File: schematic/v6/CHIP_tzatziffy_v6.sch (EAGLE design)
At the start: 53 parts, among them J1 2X20-CHIP0.8_DRILL, J3 S2B-PH-SM4-TB, Q1 NPN-DTC114YUA, Q2 PNP-DTA114YUA, U1 LMR62421, U3 DS2431P, X1 FH12-40S-0.5SH

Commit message: changed poti pins to smaller restring, added jumper for 3.3/5/vbat for DC/DC and 3.3/5 for audio amp
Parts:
- removed C8: n.a., rcl:C-EUC0805
- removed J3: S2B-PH-SM4-TB, Keyboard v0_5:S2B-PH-SM4-TB
- removed LG, RG: LSP10, solpad:LSP10
- added BGND, CHRIN, G, VBAT: (no value), wirepad:1,6/0,8
- added CHRIN_P: CHRIN, wirepad:SMD5
- added SJ2, SJ3: (no value), SparkFun-Retired:SOLDERJUMPER_2WAYT
- L+, L-, LI, LO, R+, R-, RI, RO: value LSP10 -> (none); device solpad:LSP10 -> wirepad:1,6/0,8
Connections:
- removed net N$9: C8.1, J1.VCC-5V@1
- new net N$24: CHRIN.P, CHRIN_P.P, J1.ACIN-5V
- new net VCC-5V: J1.VCC-5V@1
- net GND: now also BGND.P, G.P; no longer C8.2, J3.2, LG.MP, RG.MP
- net N$26: now also SJ2.2
- net N$32: now also L+.P; no longer L+.MP
- net N$33: now also L-.P; no longer L-.MP
- net N$34: now also R+.P; no longer R+.MP
- net N$35: now also R-.P; no longer R-.MP
- net N$41: now also LI.P, LO.P; no longer LI.MP, LO.MP
- net N$43: now also RI.P, RO.P; no longer RI.MP, RO.MP
- net VBAT_EXT: now also VBAT.P; no longer J3.1
- net VCC3V3: now also C11.2, C12.2, C15.1, PAM1.MUTE, PAM1.PVDD, PAM1.PVDD1, PAM1.VDD, SJ3.2, SJ3.3
- net VCC5V: now also SJ2.3, SJ3.1; no longer C11.2, C12.2, C15.1, PAM1.MUTE, PAM1.PVDD, PAM1.PVDD1, PAM1.VDD
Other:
- note added: "cut here ->"

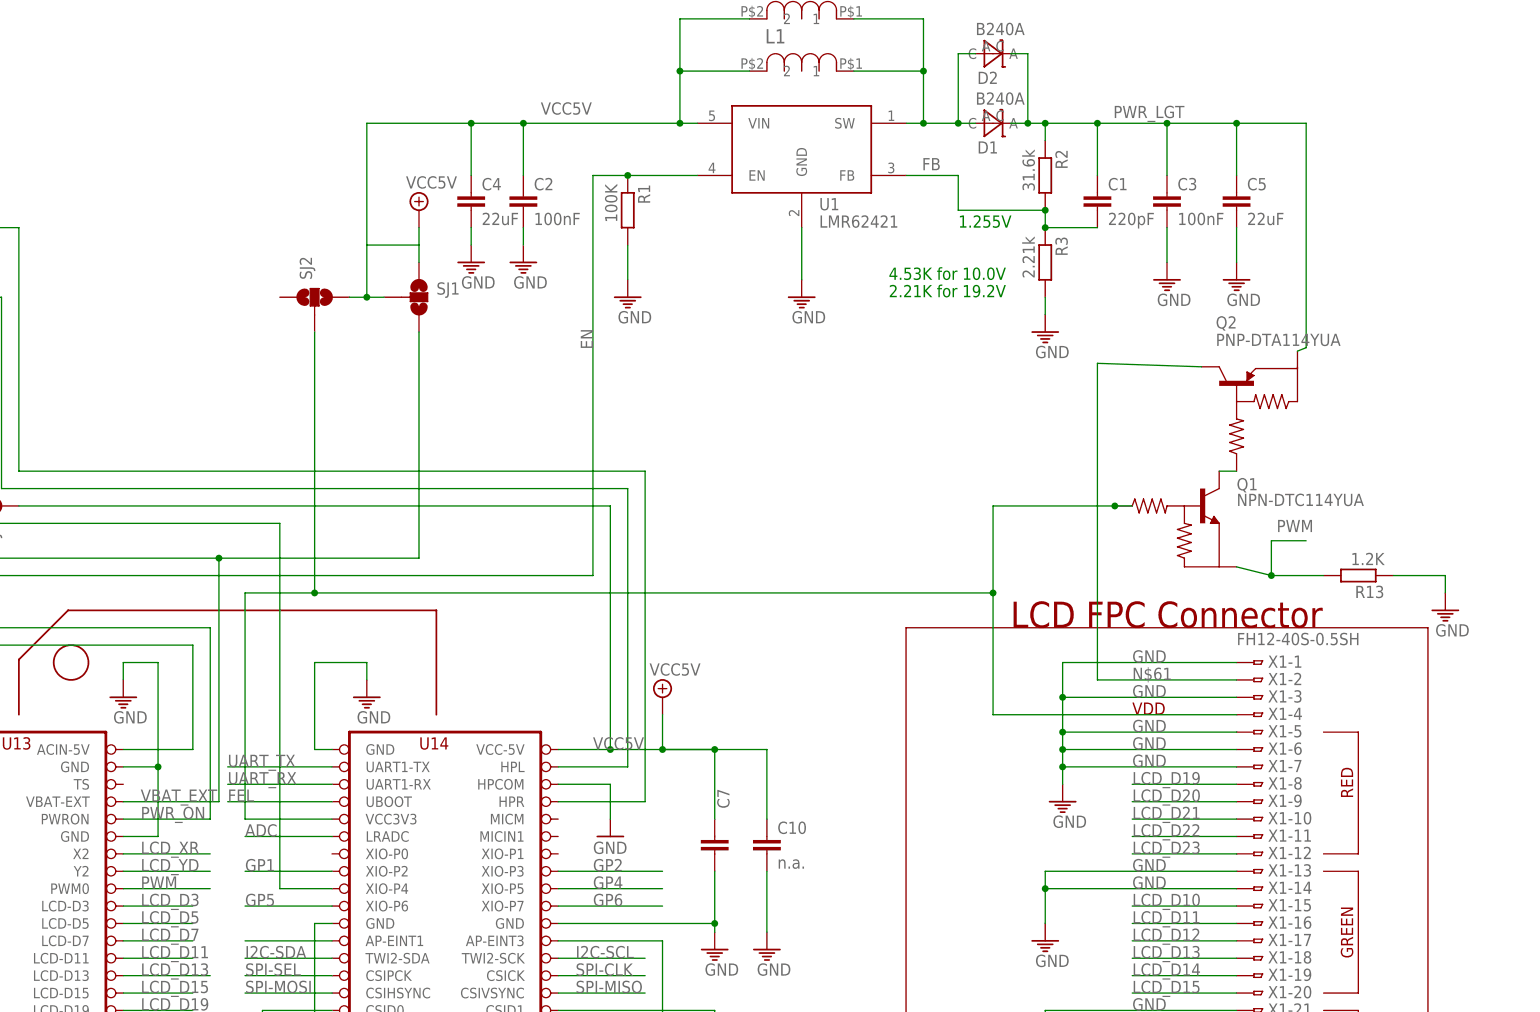
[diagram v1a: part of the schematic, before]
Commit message: replaced bipolar with mosfet circuit and relayouted
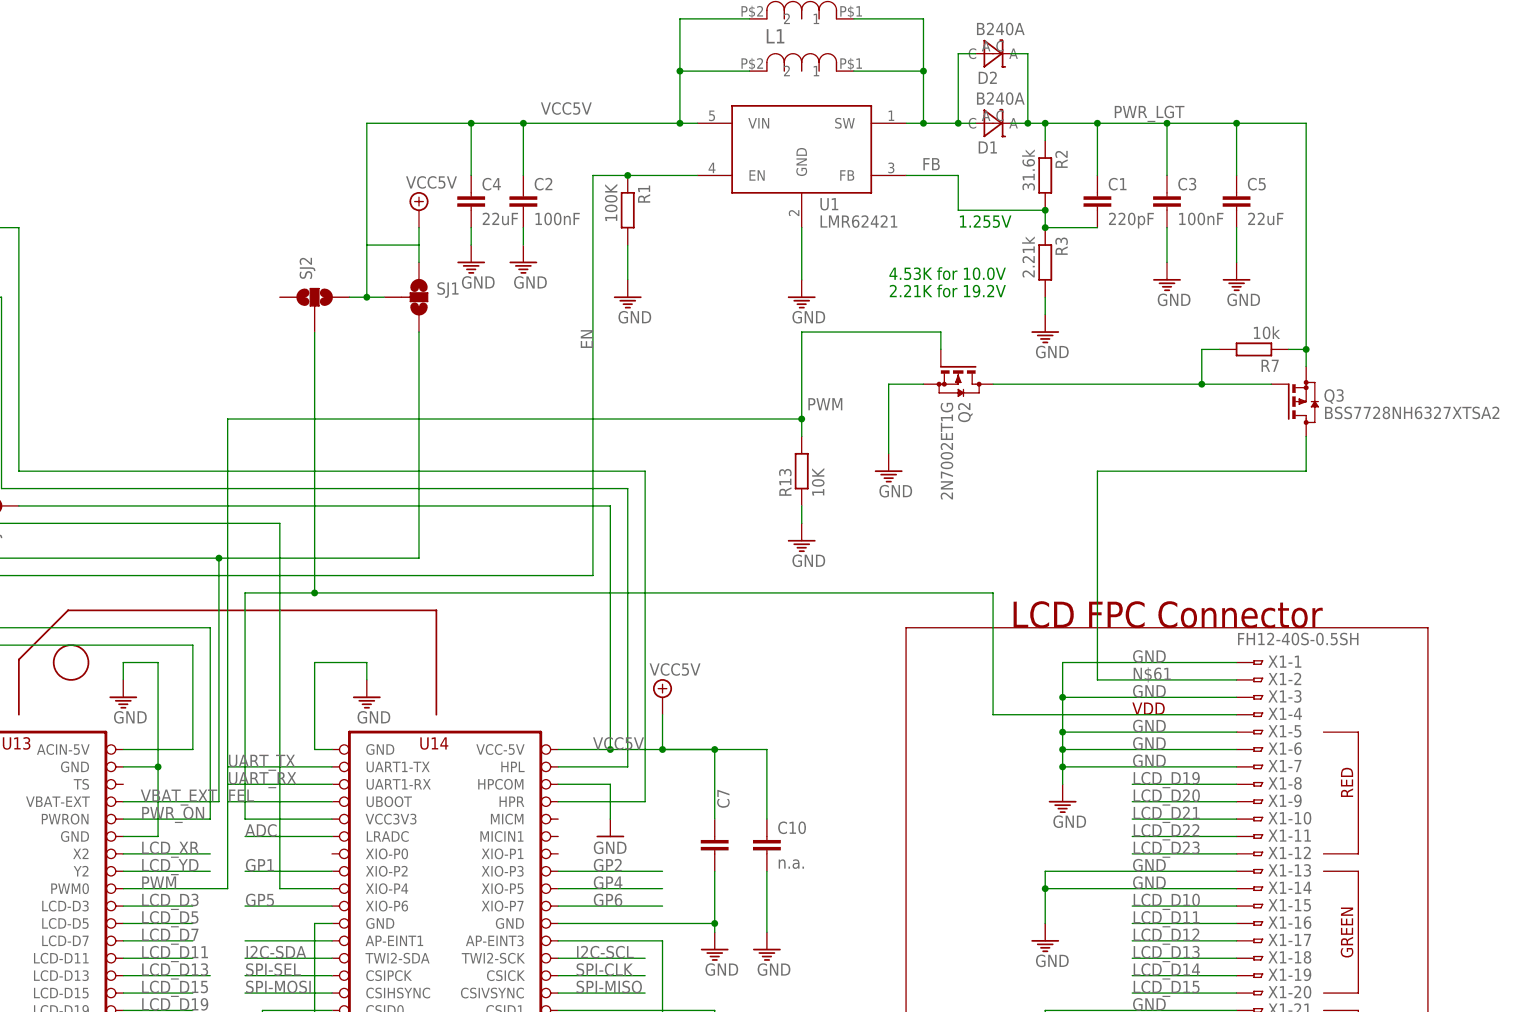
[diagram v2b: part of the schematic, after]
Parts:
- removed Q1: NPN-DTC114YUA, PocketCHIP-Components-v0.72:NPN-DTC114YUA
- added Q3: BSS7728NH6327XTSA2, transistor-small-signal:BSS84
- added R7: 10k, rcl:R-EU_M0805
- Q2: value PNP-DTA114YUA -> 2N7002ET1G; device PocketCHIP-Components-v0.72:PNP-DTA114YUA -> transistor-small-signal:BSS123
- R13: value 1.2K -> 10K
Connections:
- removed net N$63: Q1.OUT, Q2.IN
- new net N$9: Q2.D, Q3.G, R7.2
- net GND: now also Q2.S
- net N$26: no longer Q1.IN
- net N$61: now also Q3.D; no longer Q2.OUT
- net PWM: now also Q2.G; no longer Q1.GND
- net PWR_LGT: now also Q3.S, R7.1; no longer Q2.GND
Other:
- moved on the sheet: R13
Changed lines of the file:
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@@
 <part name="U3" library="Keyboard v0_5" deviceset="DS2431" device="P"/>
 <part name="D1" library="Keyboard v0_5" deviceset="DIODE_SCHTKY_B240" device="" value="B240A"/>
-<part name="Q2" library="PocketCHIP-Components-v0.72" deviceset="PNP-DTA114YUA" device=""/>
-<part name="Q1" library="PocketCHIP-Components-v0.72" deviceset="NPN-DTC114YUA" device=""/>
-<part name="R13" library="rcl" deviceset="R-EU_" device="M0805" value="1.2K"/>
+<part name="R13" library="rcl" deviceset="R-EU_" device="M0805" value="10K"/>
 <part name="U$40" library="Keyboard v0.2" deviceset="GND" device=""/>
 <part name="J1" library="JKW_CHIP" deviceset="2X20-CHIP" device="0.8_DRILL" value="2X20-CHIP0.8_DRILL"/>
@@
 <part name="VBAT" library="wirepad" deviceset="1,6/0,8" device=""/>
 <part name="CHRIN" library="wirepad" deviceset="1,6/0,8" device=""/>
+<part name="Q3" library="transistor-small-signal" deviceset="BSS84" device="" value="BSS7728NH6327XTSA2"/>
+<part name="R7" library="rcl" deviceset="R-EU_" device="M0805" value="10k"/>
+<part name="U$7" library="Keyboard v0.2" deviceset="GND" device=""/>
+<part name="Q2" library="transistor-small-signal" deviceset="BSS123" device="" value="2N7002ET1G"/>
 </parts>
 <sheets>
@@
 <instance part="U3" gate="G$1" x="246.38" y="60.96"/>
 <instance part="D1" gate="G$1" x="535.94" y="261.62"/>
-<instance part="Q2" gate="G$1" x="571.5" y="220.98" smashed="yes" rot="R90">
-<attribute name="NAME" x="568.452" y="231.648" size="1.778" layer="95"/>
-<attribute name="VALUE" x="568.452" y="229.108" size="1.778" layer="96"/>
-</instance>
-<instance part="Q1" gate="G$1" x="563.88" y="205.74" smashed="yes">
-<attribute name="NAME" x="571.5" y="208.026" size="1.778" layer="95"/>
-<attribute name="VALUE" x="571.5" y="205.74" size="1.778" layer="96"/>
-</instance>
-<instance part="R13" gate="G$1" x="589.28" y="195.58" rot="R180"/>
-<instance part="U$40" gate="M" x="601.98" y="190.5"/>
+<instance part="R13" gate="G$1" x="508" y="210.82" rot="R90"/>
+<instance part="U$40" gate="M" x="508" y="200.66"/>
 <instance part="J1" gate="G$1" x="424.18" y="147.32"/>
 <instance part="GND2" gate="1" x="406.4" y="38.1" rot="MR0"/>
@@
 <instance part="VBAT" gate="P" x="281.94" y="198.12"/>
 <instance part="CHRIN" gate="P" x="236.22" y="142.24" rot="R270"/>
+<instance part="Q3" gate="G$1" x="581.66" y="220.98"/>
+<instance part="R7" gate="G$1" x="574.04" y="228.6" rot="R180"/>
+<instance part="U$7" gate="M" x="520.7" y="210.82"/>
+<instance part="Q2" gate="G$1" x="530.86" y="223.52" rot="R270"/>
 </instances>
 <busses>
@@
 <segment>
 <pinref part="U$40" gate="M" pin="GND"/>
-<wire x1="601.98" y1="193.04" x2="601.98" y2="195.58" width="0.1524" layer="91"/>
 <pinref part="R13" gate="G$1" pin="1"/>
-<wire x1="601.98" y1="195.58" x2="594.36" y2="195.58" width="0.1524" layer="91"/>
+<wire x1="508" y1="203.2" x2="508" y2="205.74" width="0.1524" layer="91"/>
 </segment>
 <segment>
@@
 <wire x1="256.54" y1="132.08" x2="256.54" y2="139.7" width="0.1524" layer="91"/>
 </segment>
+<segment>
+<wire x1="525.78" y1="223.52" x2="520.7" y2="223.52" width="0.1524" layer="91"/>
+<wire x1="520.7" y1="223.52" x2="520.7" y2="213.36" width="0.1524" layer="91"/>
+<pinref part="U$7" gate="M" pin="GND"/>
+<pinref part="Q2" gate="G$1" pin="S"/>
+</segment>
 </net>
 <net name="I2C-SDA" class="0">
@@
 <label x="563.88" y="264.16" size="1.778" layer="95" rot="R180"/>
 <wire x1="571.5" y1="261.62" x2="581.66" y2="261.62" width="0.1524" layer="91"/>
-<wire x1="581.66" y1="261.62" x2="581.66" y2="228.854" width="0.1524" layer="91"/>
+<wire x1="581.66" y1="261.62" x2="581.66" y2="228.6" width="0.1524" layer="91"/>
 <junction x="571.5" y="261.62"/>
 <pinref part="D1" gate="G$1" pin="C"/>
+<wire x1="581.66" y1="228.6" x2="581.66" y2="226.06" width="0.1524" layer="91"/>
 <wire x1="538.48" y1="261.62" x2="541.02" y2="261.62" width="0.1524" layer="91"/>
 <wire x1="541.02" y1="261.62" x2="543.56" y2="261.62" width="0.1524" layer="91"/>
-<wire x1="581.66" y1="228.854" x2="580.39" y2="228.346" width="0.1524" layer="91"/>
-<pinref part="Q2" gate="G$1" pin="GND"/>
 <pinref part="D2" gate="G$1" pin="C"/>
 <wire x1="538.48" y1="271.78" x2="541.02" y2="271.78" width="0.1524" layer="91"/>
 <wire x1="541.02" y1="271.78" x2="541.02" y2="261.62" width="0.1524" layer="91"/>
 <junction x="541.02" y="261.62"/>
+<pinref part="Q3" gate="G$1" pin="S"/>
+<pinref part="R7" gate="G$1" pin="1"/>
+<wire x1="579.12" y1="228.6" x2="581.66" y2="228.6" width="0.1524" layer="91"/>
+<junction x="581.66" y="228.6"/>
 </segment>
 </net>
@@
 <pinref part="X1" gate="-2" pin="1"/>
 <wire x1="571.5" y1="180.34" x2="551.18" y2="180.34" width="0.1524" layer="91"/>
-<wire x1="551.18" y1="180.34" x2="551.18" y2="226.568" width="0.1524" layer="91"/>
+<wire x1="551.18" y1="180.34" x2="551.18" y2="210.82" width="0.1524" layer="91"/>
 <label x="556.26" y="180.34" size="1.778" layer="95"/>
-<pinref part="Q2" gate="G$1" pin="OUT"/>
-<wire x1="566.42" y1="226.06" x2="551.18" y2="226.568" width="0.1524" layer="91"/>
-</segment>
-</net>
-<net name="N$63" class="0">
-<segment>
-<pinref part="Q2" gate="G$1" pin="IN"/>
-<pinref part="Q1" gate="G$1" pin="OUT"/>
-<wire x1="571.5" y1="210.82" x2="568.96" y2="210.82" width="0.1524" layer="91"/>
+<pinref part="Q3" gate="G$1" pin="D"/>
+<wire x1="551.18" y1="210.82" x2="581.66" y2="210.82" width="0.1524" layer="91"/>
+<wire x1="581.66" y1="210.82" x2="581.66" y2="215.9" width="0.1524" layer="91"/>
 </segment>
 </net>
 <net name="PWM" class="0">
 <segment>
-<wire x1="408.94" y1="149.86" x2="421.64" y2="149.86" width="0.1524" layer="91"/>
+<wire x1="408.94" y1="149.86" x2="424.18" y2="149.86" width="0.1524" layer="91"/>
 <label x="411.48" y="149.86" size="1.778" layer="95" font="vector" ratio="12"/>
 <pinref part="J1" gate="G$1" pin="PWM0"/>
-</segment>
-<segment>
-<pinref part="Q1" gate="G$1" pin="GND"/>
+<wire x1="424.18" y1="149.86" x2="424.18" y2="218.44" width="0.1524" layer="91"/>
 <pinref part="R13" gate="G$1" pin="2"/>
-<wire x1="571.5" y1="196.85" x2="576.58" y2="195.58" width="0.1524" layer="91"/>
-<wire x1="576.58" y1="195.58" x2="584.2" y2="195.58" width="0.1524" layer="91"/>
-<wire x1="576.58" y1="195.58" x2="576.58" y2="200.66" width="0.1524" layer="91"/>
-<wire x1="576.58" y1="200.66" x2="581.66" y2="200.66" width="0.1524" layer="91"/>
-<junction x="576.58" y="195.58"/>
-<label x="577.342" y="201.93" size="1.778" layer="95"/>
+<label x="508.762" y="219.71" size="1.778" layer="95"/>
+<wire x1="508" y1="215.9" x2="508" y2="218.44" width="0.1524" layer="91"/>
+<wire x1="424.18" y1="218.44" x2="508" y2="218.44" width="0.1524" layer="91"/>
+<pinref part="Q2" gate="G$1" pin="G"/>
+<wire x1="528.32" y1="228.6" x2="528.32" y2="231.14" width="0.1524" layer="91"/>
+<wire x1="528.32" y1="231.14" x2="508" y2="231.14" width="0.1524" layer="91"/>
+<wire x1="508" y1="231.14" x2="508" y2="218.44" width="0.1524" layer="91"/>
+<junction x="508" y="218.44"/>
 </segment>
 </net>
@@
 <wire x1="426.72" y1="193.04" x2="436.88" y2="193.04" width="0.1524" layer="91"/>
 <wire x1="436.88" y1="193.04" x2="535.94" y2="193.04" width="0.1524" layer="91"/>
-<wire x1="535.94" y1="193.04" x2="535.94" y2="205.74" width="0.1524" layer="91"/>
 <wire x1="535.94" y1="175.26" x2="535.94" y2="193.04" width="0.1524" layer="91"/>
-<junction x="535.94" y="193.04"/>
-<wire x1="556.26" y1="205.74" x2="553.72" y2="205.74" width="0.1524" layer="91"/>
-<pinref part="Q1" gate="G$1" pin="IN"/>
-<wire x1="553.72" y1="205.74" x2="535.94" y2="205.74" width="0.1524" layer="91"/>
-<junction x="553.72" y="205.74"/>
 <wire x1="436.88" y1="193.04" x2="436.88" y2="231.14" width="0.1524" layer="91"/>
 <pinref part="SJ2" gate="G$1" pin="2"/>
@@
 </segment>
 </net>
+<net name="N$9" class="0">
+<segment>
+<pinref part="Q3" gate="G$1" pin="G"/>
+<pinref part="R7" gate="G$1" pin="2"/>
+<wire x1="576.58" y1="223.52" x2="566.42" y2="223.52" width="0.1524" layer="91"/>
+<wire x1="566.42" y1="223.52" x2="535.94" y2="223.52" width="0.1524" layer="91"/>
+<wire x1="568.96" y1="228.6" x2="566.42" y2="228.6" width="0.1524" layer="91"/>
+<wire x1="566.42" y1="228.6" x2="566.42" y2="223.52" width="0.1524" layer="91"/>
+<junction x="566.42" y="223.52"/>
+<pinref part="Q2" gate="G$1" pin="D"/>
+</segment>
+</net>
